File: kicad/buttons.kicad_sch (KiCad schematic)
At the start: 19 parts, among them U4 MAX7219, U6 CD4051B, U7 CD4051B

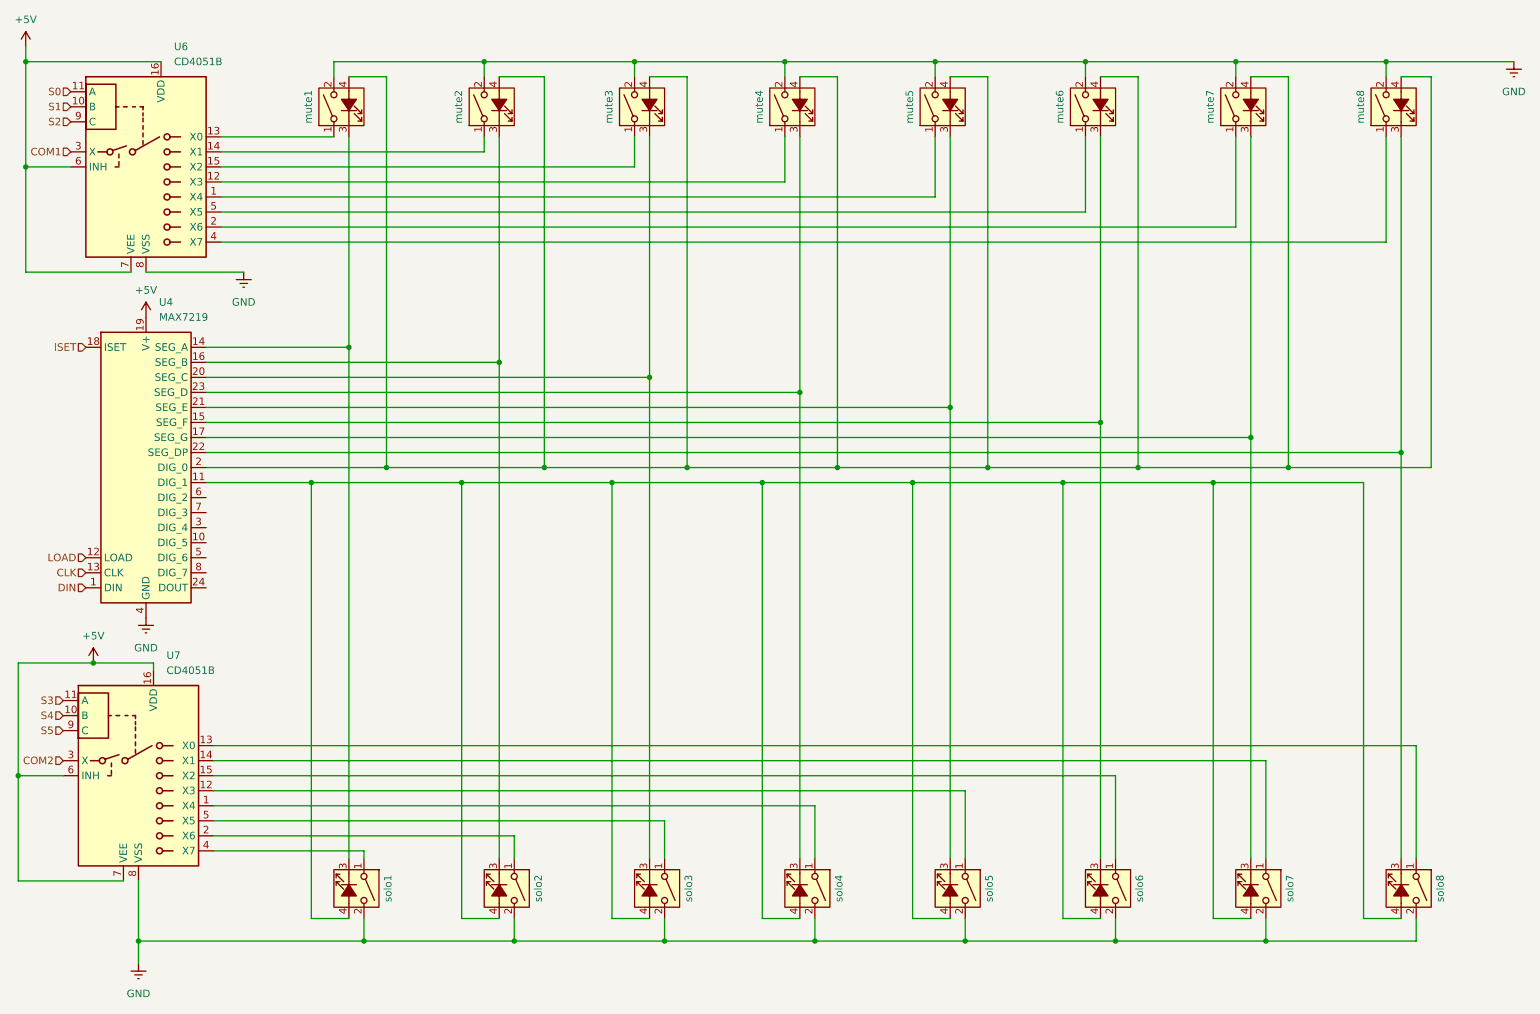
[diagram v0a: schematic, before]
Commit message: gain, meter and display sheets
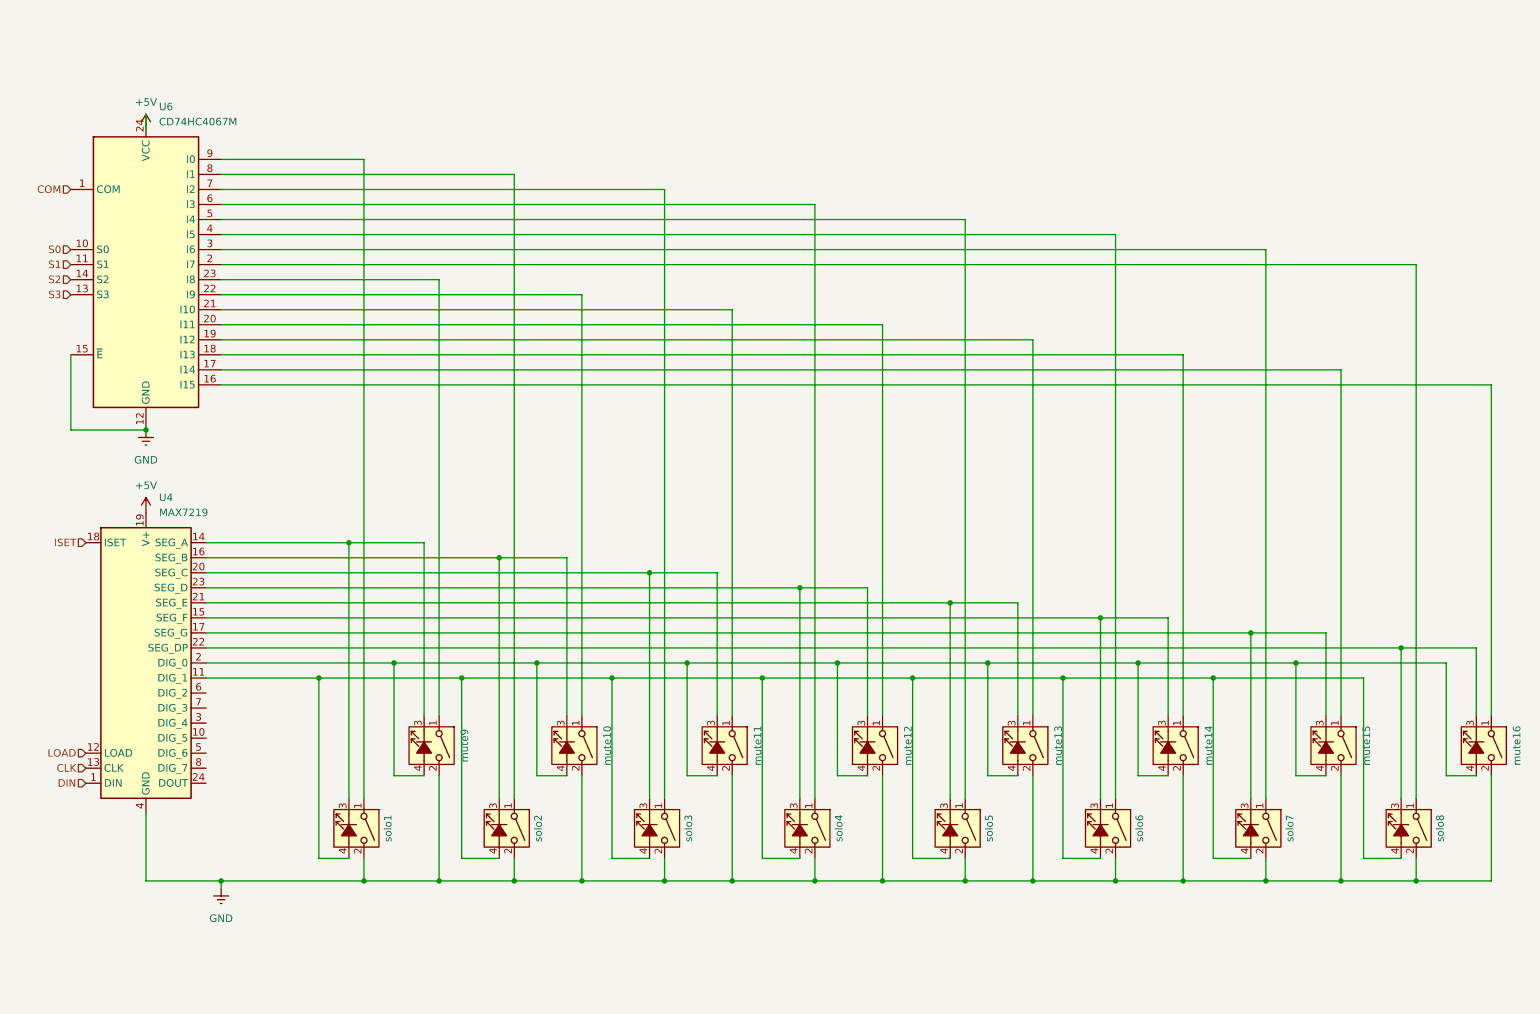
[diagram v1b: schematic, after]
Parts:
- removed U6, U7: CD4051B, symbol Analog_Switch:CD4051B
- removed mute1, mute2, mute3, mute4, mute5, mute6, mute7, mute8: SW_SPST_LED, symbol Switch:SW_SPST_LED
- added U6: CD74HC4067M, Package_SO:SOIC-24W_7.5x15.4mm_P1.27mm, symbol 74xx:CD74HC4067M
- added mute10, mute11, mute12, mute13, mute14, mute15, mute16, mute9: SW_SPST_LED, symbol Switch:SW_SPST_LED
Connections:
- net +5V: now also U6.24 (VCC)
- net GND: now also U6.12 (GND), U6.15 (~{E}), mute10.2, mute11.2, mute12.2, mute13.2, mute14.2, mute15.2, mute16.2, mute9.2
- net S0: now also U6.10 (S0)
- net S1: now also U6.11 (S1)
- net S2: now also U6.14 (S2)
- net S3: now also U6.13 (S3)
- net at U4.15 (SEG_F), solo6.3 (K): now also mute14.3 (K)
- net at U4.2 (DIG_0): now also mute10.4 (A), mute11.4 (A), mute12.4 (A), mute13.4 (A), mute14.4 (A), mute15.4 (A), mute16.4 (A), mute9.4 (A)
- net at solo3.1: now also U6.7 (I2)
- net at U4.20 (SEG_C), solo3.3 (K): now also mute11.3 (K)
- net at U4.22 (SEG_DP), solo8.3 (K): now also mute16.3 (K)
- net at solo2.1: now also U6.8 (I1)
- net at U4.16 (SEG_B), solo2.3 (K): now also mute10.3 (K)
- net at solo5.1: now also U6.5 (I4)
- net at U4.21 (SEG_E), solo5.3 (K): now also mute13.3 (K)
- net at solo1.1: now also U6.9 (I0)
- net at U4.14 (SEG_A), solo1.3 (K): now also mute9.3 (K)
- net at solo4.1: now also U6.6 (I3)
- net at solo8.1: now also U6.2 (I7)
- net at solo7.1: now also U6.3 (I6)
- net at solo6.1: now also U6.4 (I5)
- net at U4.17 (SEG_G), solo7.3 (K): now also mute15.3 (K)
- net at U4.23 (SEG_D), solo4.3 (K): now also mute12.3 (K)
- new net: U6.23 (I8), mute9.1
- new net: U6.22 (I9), mute10.1
- new net: U6.17 (I14), mute15.1
- new net: U6.16 (I15), mute16.1
- new net: U6.18 (I13), mute14.1
- new net: U6.19 (I12), mute13.1
- new net: U6.20 (I11), mute12.1
- new net: U6.21 (I10), mute11.1
- new net COM: U6.1 (COM)
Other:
- moved on the sheet: U4, solo1, solo2, solo3, solo4, solo5, solo6, solo7, solo8

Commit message: kicad updates
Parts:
- added C8, C9: 100nF, Capacitor_THT:C_Axial_L5.1mm_D3.1mm_P7.50mm_Horizontal, symbol Device:C
- added R5: R, Resistor_THT:R_Axial_DIN0207_L6.3mm_D2.5mm_P10.16mm_Horizontal, symbol Device:R
- U4: footprint (none) -> Package_DIP:DIP-24_W7.62mm_Socket
- mute10, mute11, mute12, mute13, mute14, mute15, mute16, mute9, solo1, solo2, solo3, solo4, solo5, solo6, solo7, solo8: footprint (none) -> mixer:SW_SPST_LED_9mm
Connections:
- net +5V: now also C8.2, C9.2, R5.1
- net GND: now also C8.1, C9.1
- net ISET: no longer names the net of U4.18 (ISET)
- net ISET: now also R5.2
